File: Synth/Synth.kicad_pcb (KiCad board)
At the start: 2 copper layers, 41 parts, among them Q1 PNP, Q2 NPN, Q3 PNP, Q4 NPN, U10 LM321, U11 LM321, U12 LM321, U3 LM321, U4 LM321, U5 LM321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

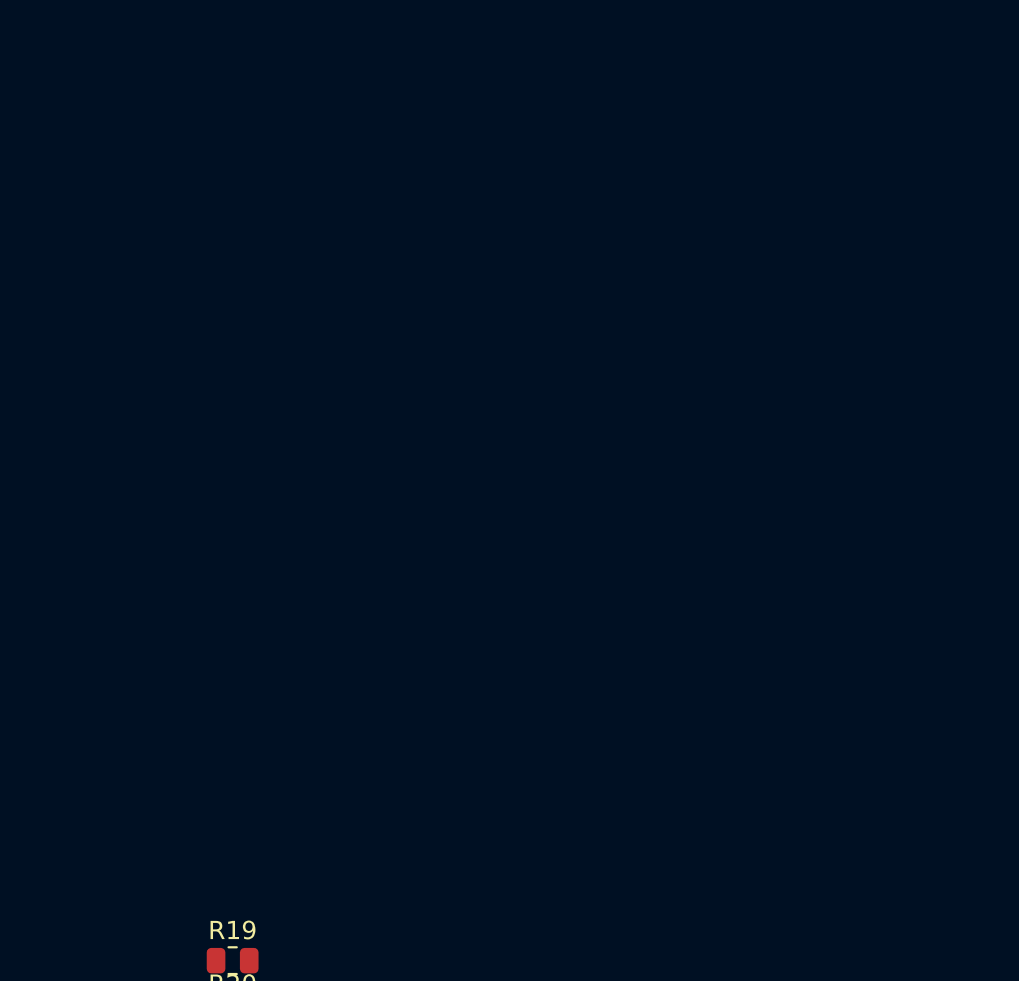
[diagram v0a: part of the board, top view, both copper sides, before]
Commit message: changed the potentiometer footprints
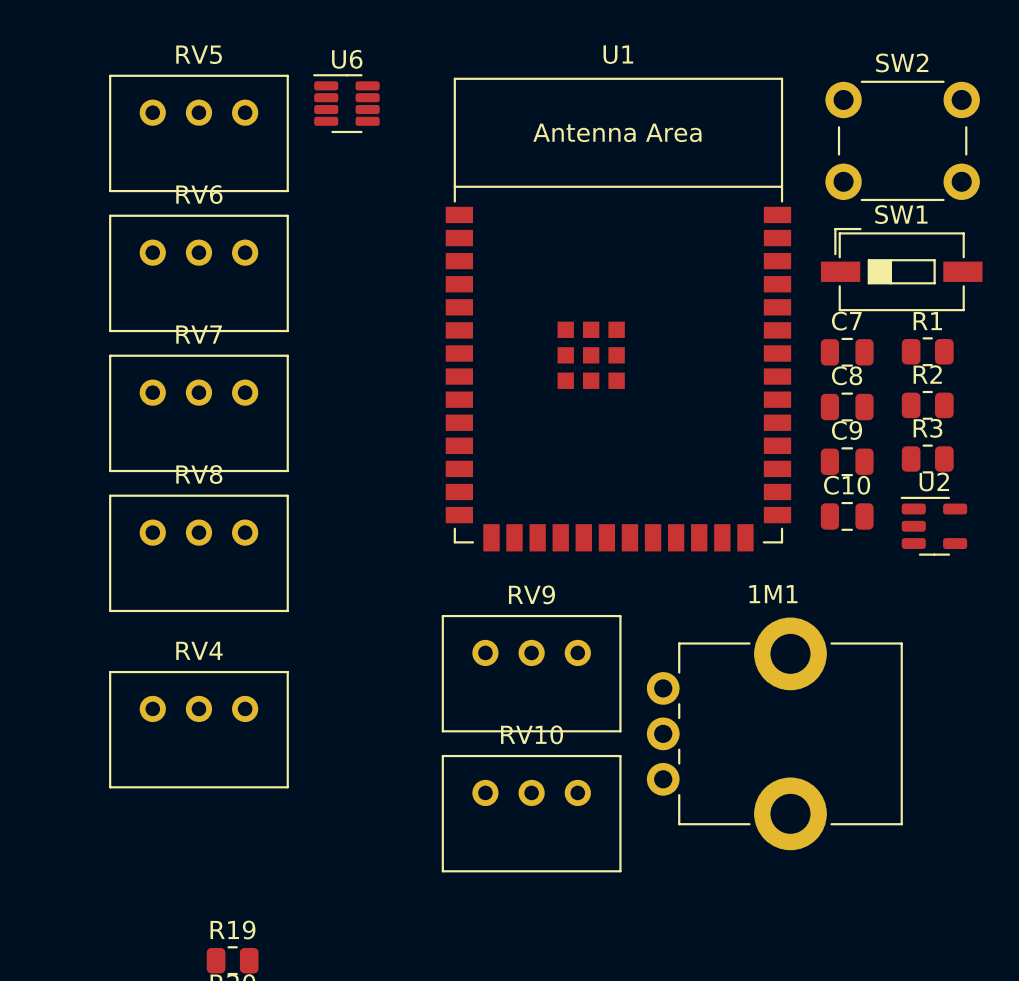
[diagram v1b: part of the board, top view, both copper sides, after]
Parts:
- added 1M1: R_Potentiometer, Potentiometer_THT:Potentiometer_Bourns_PTV09A-1_Single_Vertical, F.Cu at (173.1, 78.7)
- added C10: 1uF, Capacitor_SMD:C_0805_2012Metric, F.Cu at (183.3, 64.2)
- added C7: 0.1uF, Capacitor_SMD:C_0805_2012Metric, F.Cu at (183.3, 55.2)
- added C8: 0.1uF, Capacitor_SMD:C_0805_2012Metric, F.Cu at (183.3, 58.2)
- added C9: 0.1uF, Capacitor_SMD:C_0805_2012Metric, F.Cu at (183.3, 61.2)
- added R1: 1k, Resistor_SMD:R_0805_2012Metric, F.Cu at (187.7, 55.1)
- added R2: 1.7k, Resistor_SMD:R_0805_2012Metric, F.Cu at (187.7, 58.1)
- added R3: 10k, Resistor_SMD:R_0805_2012Metric, F.Cu at (187.7, 61.0)
- added RV10: 1M, Potentiometer_THT:Potentiometer_Bourns_3299W_Vertical, F.Cu at (168.4, 79.4)
- added RV4: 20k, Potentiometer_THT:Potentiometer_Bourns_3299W_Vertical, F.Cu at (150.1, 74.8)
- added RV5: R_Potentiometer, Potentiometer_THT:Potentiometer_Bourns_3299W_Vertical, F.Cu at (150.1, 42.0)
- added RV6: R_Potentiometer, Potentiometer_THT:Potentiometer_Bourns_3299W_Vertical, F.Cu at (150.1, 49.7)
- added RV7: R_Potentiometer, Potentiometer_THT:Potentiometer_Bourns_3299W_Vertical, F.Cu at (150.1, 57.4)
- added RV8: R_Potentiometer, Potentiometer_THT:Potentiometer_Bourns_3299W_Vertical, F.Cu at (150.1, 65.1)
- added RV9: 100k, Potentiometer_THT:Potentiometer_Bourns_3299W_Vertical, F.Cu at (168.4, 71.7)
- added SW1: Reset, Button_Switch_SMD:SW_DIP_SPSTx01_Slide_6.7x4.1mm_W6.73mm_P2.54mm_LowProfile_JPin, F.Cu at (186.3, 50.8)
- added SW2: Boot, Button_Switch_THT:SW_PUSH_6mm_H7.3mm, F.Cu at (183.1, 41.3)
- added U1: ESP32-S2-SOLO, PCM_Espressif:ESP32-S2-SOLO, F.Cu at (170.7, 55.9)
- added U2: LM321, Package_TO_SOT_SMD:SOT-23-5, F.Cu at (188.1, 64.8)
- added U6: Opamp_Dual, Package_TO_SOT_SMD:TSOT-23-8, F.Cu at (155.7, 41.5)
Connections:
- net /'ADSR' Envelope/EN_in+ renamed EN_in+
- C2 pad 2: Net-(C2-Pad2) -> LowPass Input
- C4 pad 1: Net-(C4-Pad1) -> Filter Out
- C5 pad 1: /'ADSR' Envelope/V_in+ -> V_in+
- R8 pad 1: V_in+ -> V_inW+
- U11 pad 3: V_inWF+ -> V_in_EN+
- U11 pad 4: V_inWF+ -> V_in_EN+
- U12 pad 1: V_inWF+ -> Filter Output
- U12 pad 3: V_out+ -> V_inWF+
- U12 pad 4: V_out+ -> V_inWF+
- U4 pad 2: unconnected-(U4-V--Pad2) -> GND
- U4 pad 5: unconnected-(U4-V+-Pad5) -> +12V
- U8 pad 1: /'ADSR' Envelope/V_in+ -> V_in+

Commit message: almost done w layoutgit add *
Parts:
- added JP1+1: SolderJumper_2_Open, Jumper:SolderJumper-2_P1.3mm_Bridged_RoundedPad1.0x1.5mm, F.Cu at (177.4, 43.3)
- added Q3: PNP, Package_TO_SOT_SMD:SOT-23-5_HandSoldering, F.Cu at (64.6, 92.1)
- added R4: 20k, Resistor_SMD:R_0805_2012Metric, F.Cu at (185.5, 45.9)
- added RV1: 20k, Potentiometer_THT:Potentiometer_Bourns_3299W_Vertical, F.Cu at (179.0, 52.3)
- added TP1: TestPoint, TestPoint:TestPoint_Pad_2.5x2.5mm, F.Cu at (164.7, 43.3)
- moved RV4 113.3 mm to (37.2, 65.6)
- moved R10 106.0 mm to (27.0, 82.4)
- moved Q1 102.2 mm to (25.5, 89.1)
- moved U3 97.4 mm to (33.1, 88.0)
- moved RV9 93.6 mm to (86.5, 117.0), turned to 90 degrees
- moved R8 92.4 mm to (32.1, 82.4), turned to -90 degrees
- moved R12 92.4 mm to (27.0, 95.1), turned to -90 degrees
- moved U4 88.0 mm to (39.2, 107.8)
- moved SW1 87.7 mm to (98.7, 46.9)
- moved RV5 87.1 mm to (63.1, 39.1)
- moved RV6 87.1 mm to (63.1, 46.8)
- moved RV7 87.1 mm to (63.1, 54.5)
- moved RV8 87.1 mm to (63.1, 62.2)
- moved C10 84.9 mm to (102.2, 38.8)
- moved R11 84.7 mm to (37.7, 98.7)
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- renumbered Q3 to Qr
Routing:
- net Net-(Q3-B): track 0.00 -> 58.8 mm, vias 0 -> 2
- net Net-(Q3-C): track 0.00 -> 36.2 mm, vias 0 -> 2
- net Net-(U6B-+): track 0.00 -> 34.4 mm
- net +12V: track 0.00 -> 31.3 mm, vias 0 -> 14
- net Net-(U6A-+): track 0.00 -> 30.0 mm
- net Net-(D4-A): track 0.00 -> 29.8 mm
- net Net-(Q3-E): track 0.00 -> 29.4 mm
- net Net-(U6B--): track 0.00 -> 29.1 mm
- net Net-(U7--): track 0.00 -> 23.8 mm
- net LowPass Input: track 0.00 -> 23.6 mm, vias 0 -> 2
- net Net-(U10-+): track 0.00 -> 23.6 mm
- net Net-(U3-+): track 0.00 -> 22.5 mm
- net Net-(U4--): track 0.00 -> 19.4 mm
- net Net-(U1-GPIO0): track 0.00 -> 18.7 mm
- net Net-(R23-Pad2): track 0.00 -> 17.7 mm
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- added copper zone on B.Cu, net +12V
- added copper zone on F.Cu, net GND

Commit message: made small changes, fixed DRC Errors
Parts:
- SW1: footprint Button_Switch_SMD:SW_DIP_SPSTx01_Slide_6.7x4.1mm_W6.73mm_P2.54mm_LowProfile_JPin -> Button_Switch_THT:SW_PUSH_6mm_H8mm
- SW2: footprint Button_Switch_THT:SW_PUSH_6mm_H7.3mm -> Button_Switch_THT:SW_PUSH_6mm_H8mm
- moved JP1+1 39.2 mm to (158.4, 77.7)
- moved RV1 39.2 mm to (160.0, 86.6)
- moved TP1 39.2 mm to (145.7, 77.7)
- moved R4 39.2 mm to (166.5, 80.2)
- moved SW1 9.69 mm to (91.6, 40.2)
- moved C7 1.26 mm to (138.3, 59.8), turned to -90 degrees
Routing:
- net GND: track 8.15 -> 156.7 mm, vias 1 -> 0
- net Net-(U1-EN): track 17.0 -> 28.3 mm

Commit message: Commit the changes to the thing
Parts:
- D1: value 100k -> ~
- SW1: footprint Button_Switch_THT:SW_PUSH_6mm_H8mm -> Button_Switch_SMD:SW_DIP_SPSTx01_Slide_6.7x4.1mm_W6.73mm_P2.54mm_LowProfile_JPin
- SW2: footprint Button_Switch_THT:SW_PUSH_6mm_H8mm -> Button_Switch_THT:SW_PUSH_6mm_H7.3mm
- moved RV1 46.0 mm to (119.2, 65.2)
- moved R4 44.1 mm to (125.9, 63.2)
- moved JP1+1 44.1 mm to (117.8, 60.7)
- moved TP1 44.1 mm to (105.1, 60.7)
- moved C8 20.2 mm to (92.6, 37.2)
- moved C9 20.2 mm to (92.6, 25.0)
- moved U2 20.2 mm to (100.8, 54.0)
- moved R2 20.2 mm to (100.8, 59.1)
- moved R3 20.2 mm to (92.6, 32.1)
- moved SW2 20.2 mm to (122.9, 53.8)
- moved C10 20.2 mm to (86.5, 26.0)
- moved C7 20.2 mm to (122.6, 47.1)
- moved SW1 20.2 mm to (75.9, 27.5)
- moved U1 20.2 mm to (108.3, 39.0)
- moved R1 20.2 mm to (95.2, 59.1)
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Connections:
- C1 pad 1: HighPass Input -> ESP Out
- C4 pad 1: Filter Out -> Filter Output
- C5 pad 1: V_in+ -> V_in_EN+
- R24 pad 1: EN_in+ -> V_out+
- R8 pad 1: V_inW+ -> V_inWF+
- RV8 pad 2: Filter Out -> Filter Output
- RV8 pad 3: Filter Out -> Filter Output
- U8 pad 1: V_in+ -> V_in_EN+
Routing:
- net +12V: track 31.3 -> 133.1 mm, vias 14 -> 11
- net V_out+: track 0.00 -> 55.6 mm
- net ESP Out: track 4.22 -> 57.2 mm, vias 0 -> 2
- net V_in_EN+: track 2.28 -> 50.6 mm, vias 0 -> 2
- net V_inWF+: track 2.27 -> 40.7 mm, vias 0 -> 2
- net GND: track 156.7 -> 135.2 mm, vias 0 -> 2
- net Filter Output: track 0.00 -> 15.7 mm
- net Net-(U6B--): track 29.1 -> 15.9 mm
- net Filter Out: track 11.2 -> 0.00 mm
- net V_in+: track 8.14 -> 0.00 mm
- net Net-(JP1+1-A): track 11.7 -> 7.77 mm
- net Net-(Q3-E): track 29.4 -> 30.6 mm
- net Net-(U1-EN): track 28.3 -> 27.6 mm
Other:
- board outline added: 98.9 x 101.3 mm

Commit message: fixed
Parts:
- added TP2: TestPoint, TestPoint:TestPoint_Pad_2.5x2.5mm, F.Cu at (80.7, 74.8)
- added TP3: TestPoint, TestPoint:TestPoint_Pad_2.5x2.5mm, F.Cu at (80.7, 79.4)
- added TP4: TestPoint, TestPoint:TestPoint_Pad_2.5x2.5mm, F.Cu at (85.3, 74.9)
- added TP5: TestPoint, TestPoint:TestPoint_Pad_2.5x2.5mm, F.Cu at (85.3, 79.4)
- added TP6: TestPoint, TestPoint:TestPoint_Pad_2.5x2.5mm, F.Cu at (89.8, 74.8)
- added TP7: TestPoint, TestPoint:TestPoint_Pad_2.5x2.5mm, F.Cu at (89.8, 79.4)
- moved C4 0.64 mm to (70.2, 69.9)
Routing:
- net V_out+: track 55.6 -> 124.9 mm
- net +3.3V: track 17.7 -> 72.6 mm, vias 0 -> 2
- net +12V: track 133.1 -> 186.2 mm, vias 11 -> 12
- net V_Wavefolder+: track 11.7 -> 36.2 mm
- net Filter Output: track 15.7 -> 31.3 mm, vias 0 -> 2
- net GND: track 135.2 -> 132.8 mm
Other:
- board text added: "ASDR Envelope Potentiometer 1-3"
- board text added: "Filter Potentiometers 1-4"
- board text added: "Wavefolder Potentiometer 1"

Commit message: commit
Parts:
- moved TP1 4.16 mm to (105.4, 64.8)
- moved R9 0.91 mm to (51.5, 75.0)
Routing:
- net GND: track 132.8 -> 211.1 mm
- net Net-(R9-Pad1): track 11.3 -> 13.2 mm
